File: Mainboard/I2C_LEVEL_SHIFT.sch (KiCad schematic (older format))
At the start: 6 parts, among them Q13 BSS138, Q14 BSS138

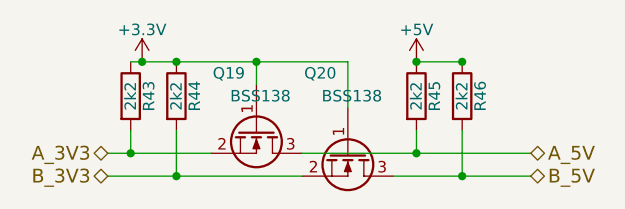
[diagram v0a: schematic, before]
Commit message: Still Missing WS2811 level shifter
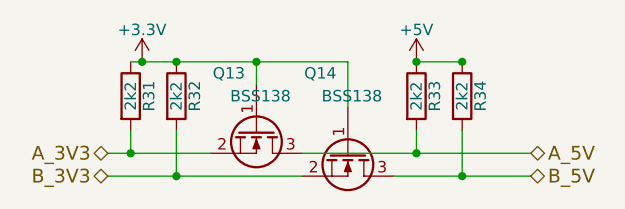
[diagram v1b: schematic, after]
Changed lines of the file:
@@
 $EndDescr
 $Comp
-L +3.3V #PWR055
+L +3.3V #PWR053
 U 1 1 56731367
 P 2900 4250
-AR Path="/56730D67/56731367" Ref="#PWR055"  Part="1"
-AR Path="/567357F7/56731367" Ref="#PWR057"  Part="1"
-AR Path="/56735BAF/56731367" Ref="#PWR059"  Part="1"
-AR Path="/56735BB5/56731367" Ref="#PWR061"  Part="1"
-F 0 "#PWR061" H 2900 4100 50  0001 C CNN
+AR Path="/56730D67/56731367" Ref="#PWR053"  Part="1"
+AR Path="/567357F7/56731367" Ref="#PWR055"  Part="1"
+AR Path="/56735BAF/56731367" Ref="#PWR057"  Part="1"
+AR Path="/56735BB5/56731367" Ref="#PWR059"  Part="1"
+F 0 "#PWR053" H 2900 4100 50  0001 C CNN
 F 1 "+3.3V" H 2900 4390 50  0000 C CNN
 F 2 "" H 2900 4250 50  0000 C CNN
@@
 AR Path="/56735BAF/56731368" Ref="R39"  Part="1"
 AR Path="/56735BB5/56731368" Ref="R43"  Part="1"
-F 0 "R43" V 2930 4400 50  0000 C CNN
+F 0 "R31" V 2930 4400 50  0000 C CNN
 F 1 "2k2" V 2850 4400 50  0000 C CNN
 F 2 "Resistors_SMD:R_0805_HandSoldering" V 2780 4400 50  0001 C CNN
@@
 AR Path="/56735BAF/56731369" Ref="R40"  Part="1"
 AR Path="/56735BB5/56731369" Ref="R44"  Part="1"
-F 0 "R44" V 3130 4400 50  0000 C CNN
+F 0 "R32" V 3130 4400 50  0000 C CNN
 F 1 "2k2" V 3050 4400 50  0000 C CNN
 F 2 "Resistors_SMD:R_0805_HandSoldering" V 2980 4400 50  0001 C CNN
@@
 AR Path="/56735BAF/5673136A" Ref="R41"  Part="1"
 AR Path="/56735BB5/5673136A" Ref="R45"  Part="1"
-F 0 "R45" V 4180 4400 50  0000 C CNN
+F 0 "R33" V 4180 4400 50  0000 C CNN
 F 1 "2k2" V 4100 4400 50  0000 C CNN
 F 2 "Resistors_SMD:R_0805_HandSoldering" V 4030 4400 50  0001 C CNN
@@
 AR Path="/56735BAF/5673136B" Ref="R42"  Part="1"
 AR Path="/56735BB5/5673136B" Ref="R46"  Part="1"
-F 0 "R46" V 4380 4400 50  0000 C CNN
+F 0 "R34" V 4380 4400 50  0000 C CNN
 F 1 "2k2" V 4300 4400 50  0000 C CNN
 F 2 "Resistors_SMD:R_0805_HandSoldering" V 4230 4400 50  0001 C CNN
@@
 $EndComp
 $Comp
-L +5V #PWR056
+L +5V #PWR054
 U 1 1 5673136C
 P 4100 4250
-AR Path="/56730D67/5673136C" Ref="#PWR056"  Part="1"
-AR Path="/567357F7/5673136C" Ref="#PWR058"  Part="1"
-AR Path="/56735BAF/5673136C" Ref="#PWR060"  Part="1"
-AR Path="/56735BB5/5673136C" Ref="#PWR062"  Part="1"
-F 0 "#PWR062" H 4100 4100 50  0001 C CNN
+AR Path="/56730D67/5673136C" Ref="#PWR054"  Part="1"
+AR Path="/567357F7/5673136C" Ref="#PWR056"  Part="1"
+AR Path="/56735BAF/5673136C" Ref="#PWR058"  Part="1"
+AR Path="/56735BB5/5673136C" Ref="#PWR060"  Part="1"
+F 0 "#PWR054" H 4100 4100 50  0001 C CNN
 F 1 "+5V" H 4100 4390 50  0000 C CNN
 F 2 "" H 4100 4250 50  0000 C CNN
@@
 AR Path="/56735BAF/56761BF8" Ref="Q17"  Part="1"
 AR Path="/56735BB5/56761BF8" Ref="Q19"  Part="1"
-F 0 "Q19" V 3150 4500 50  0000 R CNN
+F 0 "Q13" V 3150 4500 50  0000 R CNN
 F 1 "BSS138" V 3250 4700 50  0000 R CNN
 F 2 "TO_SOT_Packages_SMD:SOT-23_Handsoldering" H 3600 4650 50  0001 C CNN
@@
 AR Path="/56735BAF/56761CA5" Ref="Q18"  Part="1"
 AR Path="/56735BB5/56761CA5" Ref="Q20"  Part="1"
-F 0 "Q20" V 3450 4600 50  0000 R CNN
+F 0 "Q14" V 3450 4600 50  0000 R CNN
 F 1 "BSS138" V 3550 4800 50  0000 R CNN
 F 2 "TO_SOT_Packages_SMD:SOT-23_Handsoldering" H 4000 4750 50  0001 C CNN

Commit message: Added 74HC04 buffer to WS2811 outputs
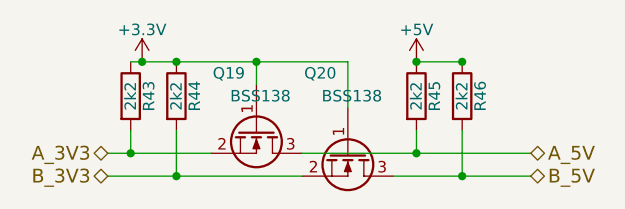
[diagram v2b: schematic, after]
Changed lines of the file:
@@
 $Descr A4 11693 8268
 encoding utf-8
-Sheet 11 14
+Sheet 14 14
 Title ""
 Date ""
@@
 $EndDescr
 $Comp
-L +3.3V #PWR053
+L +3.3V #PWR059
 U 1 1 56731367
 P 2900 4250
-AR Path="/56730D67/56731367" Ref="#PWR053"  Part="1"
-AR Path="/567357F7/56731367" Ref="#PWR055"  Part="1"
-AR Path="/56735BAF/56731367" Ref="#PWR057"  Part="1"
-AR Path="/56735BB5/56731367" Ref="#PWR059"  Part="1"
-F 0 "#PWR053" H 2900 4100 50  0001 C CNN
+AR Path="/56730D67/56731367" Ref="#PWR059"  Part="1"
+AR Path="/567357F7/56731367" Ref="#PWR061"  Part="1"
+AR Path="/56735BAF/56731367" Ref="#PWR063"  Part="1"
+AR Path="/56735BB5/56731367" Ref="#PWR065"  Part="1"
+F 0 "#PWR065" H 2900 4100 50  0001 C CNN
 F 1 "+3.3V" H 2900 4390 50  0000 C CNN
 F 2 "" H 2900 4250 50  0000 C CNN
@@
 AR Path="/56735BAF/56731368" Ref="R39"  Part="1"
 AR Path="/56735BB5/56731368" Ref="R43"  Part="1"
-F 0 "R31" V 2930 4400 50  0000 C CNN
+F 0 "R43" V 2930 4400 50  0000 C CNN
 F 1 "2k2" V 2850 4400 50  0000 C CNN
 F 2 "Resistors_SMD:R_0805_HandSoldering" V 2780 4400 50  0001 C CNN
@@
 AR Path="/56735BAF/56731369" Ref="R40"  Part="1"
 AR Path="/56735BB5/56731369" Ref="R44"  Part="1"
-F 0 "R32" V 3130 4400 50  0000 C CNN
+F 0 "R44" V 3130 4400 50  0000 C CNN
 F 1 "2k2" V 3050 4400 50  0000 C CNN
 F 2 "Resistors_SMD:R_0805_HandSoldering" V 2980 4400 50  0001 C CNN
@@
 AR Path="/56735BAF/5673136A" Ref="R41"  Part="1"
 AR Path="/56735BB5/5673136A" Ref="R45"  Part="1"
-F 0 "R33" V 4180 4400 50  0000 C CNN
+F 0 "R45" V 4180 4400 50  0000 C CNN
 F 1 "2k2" V 4100 4400 50  0000 C CNN
 F 2 "Resistors_SMD:R_0805_HandSoldering" V 4030 4400 50  0001 C CNN
@@
 AR Path="/56735BAF/5673136B" Ref="R42"  Part="1"
 AR Path="/56735BB5/5673136B" Ref="R46"  Part="1"
-F 0 "R34" V 4380 4400 50  0000 C CNN
+F 0 "R46" V 4380 4400 50  0000 C CNN
 F 1 "2k2" V 4300 4400 50  0000 C CNN
 F 2 "Resistors_SMD:R_0805_HandSoldering" V 4230 4400 50  0001 C CNN
@@
 $EndComp
 $Comp
-L +5V #PWR054
+L +5V #PWR060
 U 1 1 5673136C
 P 4100 4250
-AR Path="/56730D67/5673136C" Ref="#PWR054"  Part="1"
-AR Path="/567357F7/5673136C" Ref="#PWR056"  Part="1"
-AR Path="/56735BAF/5673136C" Ref="#PWR058"  Part="1"
-AR Path="/56735BB5/5673136C" Ref="#PWR060"  Part="1"
-F 0 "#PWR054" H 4100 4100 50  0001 C CNN
+AR Path="/56730D67/5673136C" Ref="#PWR060"  Part="1"
+AR Path="/567357F7/5673136C" Ref="#PWR062"  Part="1"
+AR Path="/56735BAF/5673136C" Ref="#PWR064"  Part="1"
+AR Path="/56735BB5/5673136C" Ref="#PWR066"  Part="1"
+F 0 "#PWR066" H 4100 4100 50  0001 C CNN
 F 1 "+5V" H 4100 4390 50  0000 C CNN
 F 2 "" H 4100 4250 50  0000 C CNN
@@
 AR Path="/56735BAF/56761BF8" Ref="Q17"  Part="1"
 AR Path="/56735BB5/56761BF8" Ref="Q19"  Part="1"
-F 0 "Q13" V 3150 4500 50  0000 R CNN
+F 0 "Q19" V 3150 4500 50  0000 R CNN
 F 1 "BSS138" V 3250 4700 50  0000 R CNN
 F 2 "TO_SOT_Packages_SMD:SOT-23_Handsoldering" H 3600 4650 50  0001 C CNN
@@
 AR Path="/56735BAF/56761CA5" Ref="Q18"  Part="1"
 AR Path="/56735BB5/56761CA5" Ref="Q20"  Part="1"
-F 0 "Q14" V 3450 4600 50  0000 R CNN
+F 0 "Q20" V 3450 4600 50  0000 R CNN
 F 1 "BSS138" V 3550 4800 50  0000 R CNN
 F 2 "TO_SOT_Packages_SMD:SOT-23_Handsoldering" H 4000 4750 50  0001 C CNN

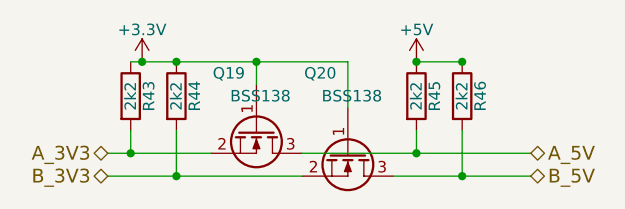
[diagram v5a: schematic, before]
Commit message: Added 8 additional Mosfet channels, cleaned up rouing a bit
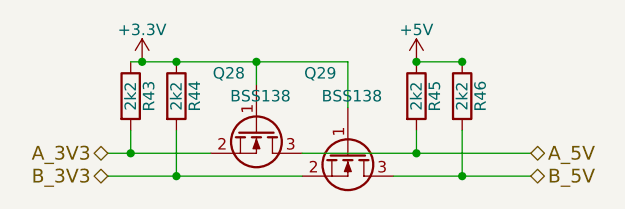
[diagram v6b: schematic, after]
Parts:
- renumbered Q13 to Q22, Q14 to Q23
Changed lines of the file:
@@
 $Descr A4 11693 8268
 encoding utf-8
-Sheet 11 19
+Sheet 4 27
 Title ""
 Date ""
@@
 $EndDescr
 $Comp
-L +3.3V #PWR040
+L +3.3V #PWR045
 U 1 1 56731367
 P 2900 4250
-AR Path="/56730D67/56731367" Ref="#PWR040"  Part="1"
-AR Path="/567357F7/56731367" Ref="#PWR042"  Part="1"
-AR Path="/56735BAF/56731367" Ref="#PWR044"  Part="1"
-AR Path="/56735BB5/56731367" Ref="#PWR046"  Part="1"
-F 0 "#PWR046" H 2900 4100 50  0001 C CNN
+AR Path="/56730D67/56731367" Ref="#PWR045"  Part="1"
+AR Path="/567357F7/56731367" Ref="#PWR047"  Part="1"
+AR Path="/56735BAF/56731367" Ref="#PWR049"  Part="1"
+AR Path="/56735BB5/56731367" Ref="#PWR051"  Part="1"
+F 0 "#PWR051" H 2900 4100 50  0001 C CNN
 F 1 "+3.3V" H 2900 4390 50  0000 C CNN
 F 2 "" H 2900 4250 50  0000 C CNN
@@
 $EndComp
 $Comp
-L +5V #PWR041
+L +5V #PWR046
 U 1 1 5673136C
 P 4100 4250
-AR Path="/56730D67/5673136C" Ref="#PWR041"  Part="1"
-AR Path="/567357F7/5673136C" Ref="#PWR043"  Part="1"
-AR Path="/56735BAF/5673136C" Ref="#PWR045"  Part="1"
-AR Path="/56735BB5/5673136C" Ref="#PWR047"  Part="1"
-F 0 "#PWR047" H 4100 4100 50  0001 C CNN
+AR Path="/56730D67/5673136C" Ref="#PWR046"  Part="1"
+AR Path="/567357F7/5673136C" Ref="#PWR048"  Part="1"
+AR Path="/56735BAF/5673136C" Ref="#PWR050"  Part="1"
+AR Path="/56735BB5/5673136C" Ref="#PWR052"  Part="1"
+F 0 "#PWR052" H 4100 4100 50  0001 C CNN
 F 1 "+5V" H 4100 4390 50  0000 C CNN
 F 2 "" H 4100 4250 50  0000 C CNN
@@
 Connection ~ 2900 4250
 $Comp
-L Q_NMOS_GSD Q13
+L Q_NMOS_GSD Q22
 U 1 1 56761BF8
 P 3400 4550
-AR Path="/56730D67/56761BF8" Ref="Q13"  Part="1"
-AR Path="/567357F7/56761BF8" Ref="Q15"  Part="1"
-AR Path="/56735BAF/56761BF8" Ref="Q17"  Part="1"
-AR Path="/56735BB5/56761BF8" Ref="Q19"  Part="1"
-F 0 "Q19" V 3150 4500 50  0000 R CNN
+AR Path="/56730D67/56761BF8" Ref="Q22"  Part="1"
+AR Path="/567357F7/56761BF8" Ref="Q24"  Part="1"
+AR Path="/56735BAF/56761BF8" Ref="Q26"  Part="1"
+AR Path="/56735BB5/56761BF8" Ref="Q28"  Part="1"
+F 0 "Q28" V 3150 4500 50  0000 R CNN
 F 1 "BSS138" V 3250 4700 50  0000 R CNN
 F 2 "TO_SOT_Packages_SMD:SOT-23_Handsoldering" H 3600 4650 50  0001 C CNN
@@
 $EndComp
 $Comp
-L Q_NMOS_GSD Q14
+L Q_NMOS_GSD Q23
 U 1 1 56761CA5
 P 3800 4650
-AR Path="/56730D67/56761CA5" Ref="Q14"  Part="1"
-AR Path="/567357F7/56761CA5" Ref="Q16"  Part="1"
-AR Path="/56735BAF/56761CA5" Ref="Q18"  Part="1"
-AR Path="/56735BB5/56761CA5" Ref="Q20"  Part="1"
-F 0 "Q20" V 3450 4600 50  0000 R CNN
+AR Path="/56730D67/56761CA5" Ref="Q23"  Part="1"
+AR Path="/567357F7/56761CA5" Ref="Q25"  Part="1"
+AR Path="/56735BAF/56761CA5" Ref="Q27"  Part="1"
+AR Path="/56735BB5/56761CA5" Ref="Q29"  Part="1"
+F 0 "Q29" V 3450 4600 50  0000 R CNN
 F 1 "BSS138" V 3550 4800 50  0000 R CNN
 F 2 "TO_SOT_Packages_SMD:SOT-23_Handsoldering" H 4000 4750 50  0001 C CNN
